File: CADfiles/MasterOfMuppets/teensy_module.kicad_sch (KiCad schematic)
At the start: 1 part, among them T1 Teensy4.1

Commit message: PCB Preps
Re-assigned footprints;
Placed all symbols in the middle;
Removed instruction to ignore the PCB in the README.manahmanah;
Added a generic placement recommendation file from Sir. Claude;
Ready to start the design;
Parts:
- T1: footprint teensy.pretty-master:Teensy41 -> Teensy:Teensy41
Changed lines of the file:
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@@
 			)
 		)
-		(property "Footprint" "teensy.pretty-master:Teensy41"
+		(property "Footprint" "Teensy:Teensy41"
 			(at 87.63 105.41 0)
 			(effects

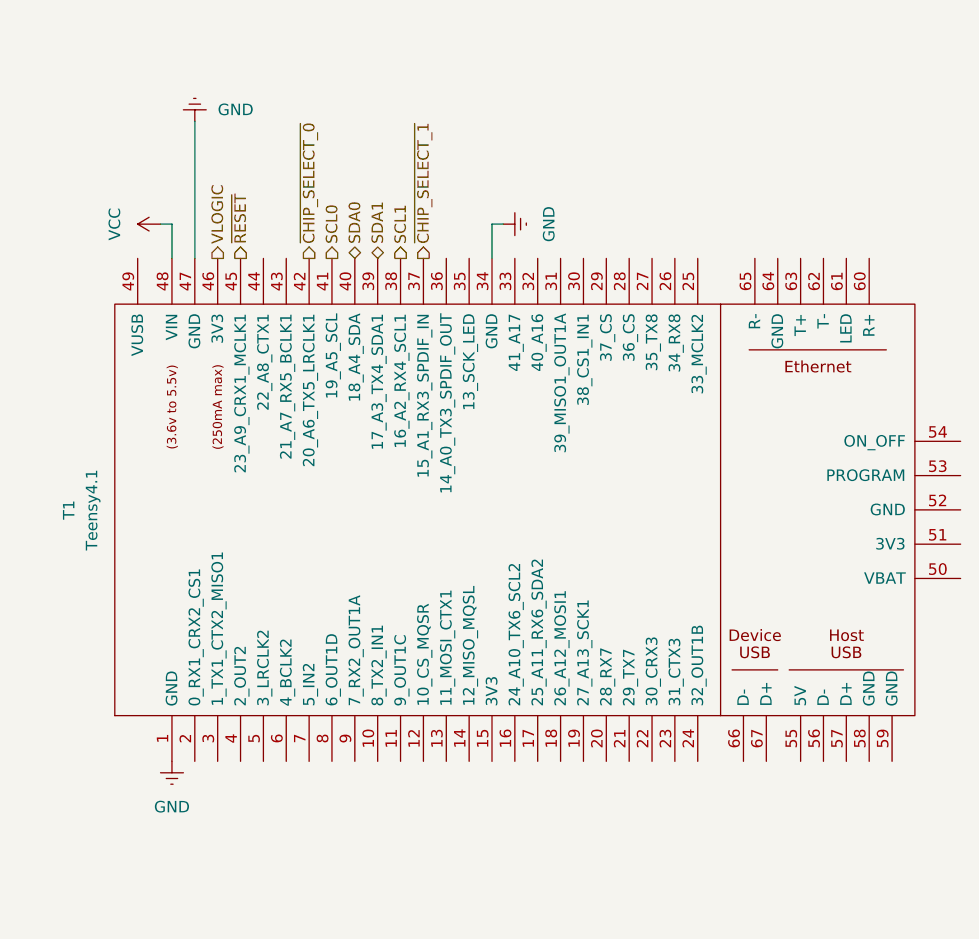
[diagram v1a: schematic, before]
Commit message: Pin configuration
The current prototype board has DAC0 mapped to Wire2 and DAC1 mapped to Wire1. The schematics were updated to reflect it.
Added chip select in the firmware for AD5593R using the address pin as a selector.
Next steps: update Claude's knowledge about it.
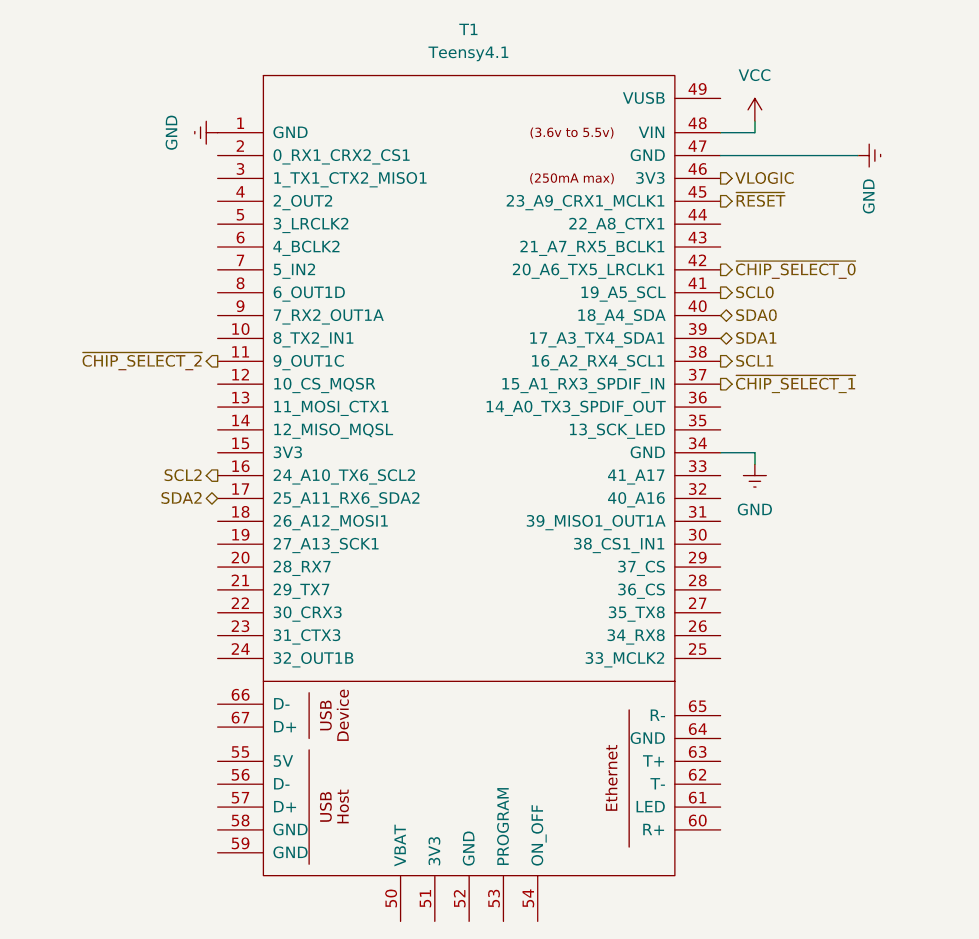
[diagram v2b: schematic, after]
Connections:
- net ~{CHIP_SELECT_2}: now reaches T1.11 (9_OUT1C)
- net SCL2: now reaches T1.16 (24_A10_TX6_SCL2)
- net SDA2: now reaches T1.17 (25_A11_RX6_SDA2)
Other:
- moved on the sheet: T1
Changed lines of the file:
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@@
 	(wire
 		(pts
-			(xy 43.18 63.5) (xy 43.18 67.31)
+			(xy 107.95 53.34) (xy 104.14 53.34)
 		)
 		(stroke
@@
 	(wire
 		(pts
-			(xy 45.72 52.07) (xy 45.72 67.31)
+			(xy 119.38 55.88) (xy 104.14 55.88)
 		)
 		(stroke
@@
 	(wire
 		(pts
-			(xy 78.74 63.5) (xy 80.01 63.5)
+			(xy 107.95 88.9) (xy 107.95 90.17)
 		)
 		(stroke
@@
 	(wire
 		(pts
-			(xy 78.74 67.31) (xy 78.74 63.5)
+			(xy 104.14 88.9) (xy 107.95 88.9)
 		)
 		(stroke
@@
 	(wire
 		(pts
-			(xy 41.91 63.5) (xy 43.18 63.5)
+			(xy 107.95 52.07) (xy 107.95 53.34)
 		)
 		(stroke
@@
 	(hierarchical_label "SDA0"
 		(shape bidirectional)
-		(at 63.5 67.31 90)
+		(at 104.14 73.66 0)
 		(effects
 			(font
@@
 	(hierarchical_label "~{RESET}"
 		(shape output)
-		(at 50.8 67.31 90)
+		(at 104.14 60.96 0)
 		(effects
 			(font
@@
 	(hierarchical_label "VLOGIC"
 		(shape output)
-		(at 48.26 67.31 90)
+		(at 104.14 58.42 0)
 		(effects
 			(font
@@
 	(hierarchical_label "SCL0"
 		(shape output)
-		(at 60.96 67.31 90)
+		(at 104.14 71.12 0)
 		(effects
 			(font
@@
 	(hierarchical_label "SDA1"
 		(shape bidirectional)
-		(at 66.04 67.31 90)
-		(effects
-			(font
-				(size 1.27 1.27)
-			)
-			(justify left)
+		(at 104.14 76.2 0)
+		(effects
+			(font
+				(size 1.27 1.27)
+			)
+			(justify left)
+		)
+	)
+	(hierarchical_label "SDA2"
+		(shape bidirectional)
+		(at 48.26 93.98 180)
+		(effects
+			(font
+				(size 1.27 1.27)
+			)
+			(justify right)
+		)
+	)
+	(hierarchical_label "SCL2"
+		(shape output)
+		(at 48.26 91.44 180)
+		(effects
+			(font
+				(size 1.27 1.27)
+			)
+			(justify right)
 		)
 	)
 	(hierarchical_label "~{CHIP_SELECT_1}"
 		(shape output)
-		(at 71.12 67.31 90)
+		(at 104.14 81.28 0)
 		(effects
 			(font
@@
 	(hierarchical_label "~{CHIP_SELECT_0}"
 		(shape output)
-		(at 58.42 67.31 90)
-		(effects
-			(font
-				(size 1.27 1.27)
-			)
-			(justify left)
+		(at 104.14 68.58 0)
+		(effects
+			(font
+				(size 1.27 1.27)
+			)
+			(justify left)
+		)
+	)
+	(hierarchical_label "~{CHIP_SELECT_2}"
+		(shape output)
+		(at 48.26 78.74 180)
+		(effects
+			(font
+				(size 1.27 1.27)
+			)
+			(justify right)
 		)
 	)
 	(hierarchical_label "SCL1"
 		(shape output)
-		(at 68.58 67.31 90)
+		(at 104.14 78.74 0)
 		(effects
 			(font
@@
 	(symbol
 		(lib_id "power:GNDREF")
-		(at 45.72 52.07 180)
+		(at 119.38 55.88 90)
 		(unit 1)
 		(exclude_from_sim no)
@@
 		(fields_autoplaced yes)
 		(property "Reference" "#PWR09"
-			(at 45.72 45.72 0)
+			(at 125.73 55.88 0)
 			(effects
 				(font
@@
 		)
 		(property "Value" "GND"
-			(at 48.26 50.7999 0)
+			(at 120.6501 58.42 0)
 			(effects
 				(font
@@
 		)
 		(property "Footprint" ""
-			(at 45.72 52.07 0)
+			(at 119.38 55.88 0)
 			(effects
 				(font
@@
 		)
 		(property "Datasheet" ""
-			(at 45.72 52.07 0)
+			(at 119.38 55.88 0)
 			(effects
 				(font
@@
 		)
 		(property "Description" "Power symbol creates a global label with name \"GNDREF\" , reference supply ground"
-			(at 45.72 52.07 0)
+			(at 119.38 55.88 0)
 			(effects
 				(font
@@
 	(symbol
 		(lib_id "teensy:Teensy4.1")
-		(at 97.79 95.25 90)
+		(at 76.2 107.95 0)
 		(unit 1)
 		(exclude_from_sim no)
@@
 		(fields_autoplaced yes)
 		(property "Reference" "T1"
-			(at 31.75 95.25 0)
+			(at 76.2 41.91 0)
 			(effects
 				(font
@@
 		)
 		(property "Value" "Teensy4.1"
-			(at 34.29 95.25 0)
+			(at 76.2 44.45 0)
 			(effects
 				(font
@@
 		)
 		(property "Footprint" "Teensy:Teensy41"
-			(at 87.63 105.41 0)
+			(at 66.04 97.79 0)
 			(effects
 				(font
@@
 		)
 		(property "Datasheet" ""
-			(at 87.63 105.41 0)
+			(at 66.04 97.79 0)
 			(effects
 				(font
@@
 		)
 		(property "Description" ""
-			(at 97.79 95.25 0)
+			(at 76.2 107.95 0)
 			(effects
 				(font
@@
 		)
 		(property "Manufacturer" ""
-			(at 97.79 95.25 0)
+			(at 76.2 107.95 0)
 			(effects
 				(font
@@
 		)
 		(property "Part Number" ""
-			(at 97.79 95.25 0)
+			(at 76.2 107.95 0)
 			(effects
 				(font
@@
 		)
 		(property "Specifications" ""
-			(at 97.79 95.25 0)
+			(at 76.2 107.95 0)
 			(effects
 				(font
@@
 	(symbol
 		(lib_id "power:GNDREF")
-		(at 80.01 63.5 90)
+		(at 107.95 90.17 0)
 		(unit 1)
 		(exclude_from_sim no)
@@
 		(fields_autoplaced yes)
 		(property "Reference" "#PWR010"
-			(at 86.36 63.5 0)
+			(at 107.95 96.52 0)
 			(effects
 				(font
@@
 		)
 		(property "Value" "GND"
-			(at 85.09 63.5 0)
+			(at 107.95 95.25 0)
 			(effects
 				(font
@@
 		)
 		(property "Footprint" ""
-			(at 80.01 63.5 0)
+			(at 107.95 90.17 0)
 			(effects
 				(font
@@
 		)
 		(property "Datasheet" ""
-			(at 80.01 63.5 0)
+			(at 107.95 90.17 0)
 			(effects
 				(font
@@
 		)
 		(property "Description" "Power symbol creates a global label with name \"GNDREF\" , reference supply ground"
-			(at 80.01 63.5 0)
+			(at 107.95 90.17 0)
 			(effects
 				(font
@@
 	(symbol
 		(lib_id "power:+5V")
-		(at 41.91 63.5 90)
+		(at 107.95 52.07 0)
 		(unit 1)
 		(exclude_from_sim no)
@@
 		(fields_autoplaced yes)
 		(property "Reference" "#PWR07"
-			(at 45.72 63.5 0)
+			(at 107.95 55.88 0)
 			(effects
 				(font
@@
 		)
 		(property "Value" "VCC"
-			(at 36.83 63.5 0)
+			(at 107.95 46.99 0)
 			(effects
 				(font
@@
 		)
 		(property "Footprint" ""
-			(at 41.91 63.5 0)
+			(at 107.95 52.07 0)
 			(effects
 				(font
@@
 		)
 		(property "Datasheet" ""
-			(at 41.91 63.5 0)
+			(at 107.95 52.07 0)
 			(effects
 				(font
@@
 		)
 		(property "Description" "Power symbol creates a global label with name \"+5V\""
-			(at 41.91 63.5 0)
+			(at 107.95 52.07 0)
 			(effects
 				(font
@@
 	(symbol
 		(lib_id "power:GNDREF")
-		(at 43.18 123.19 0)
+		(at 48.26 53.34 270)
 		(unit 1)
 		(exclude_from_sim no)
@@
 		(fields_autoplaced yes)
 		(property "Reference" "#PWR08"
-			(at 43.18 129.54 0)
+			(at 41.91 53.34 0)
 			(effects
 				(font
@@
 		)
 		(property "Value" "GND"
-			(at 43.18 128.27 0)
+			(at 43.18 53.34 0)
 			(effects
 				(font
@@
 		)
 		(property "Footprint" ""
-			(at 43.18 123.19 0)
+			(at 48.26 53.34 0)
 			(effects
 				(font
@@
 		)
 		(property "Datasheet" ""
-			(at 43.18 123.19 0)
+			(at 48.26 53.34 0)
 			(effects
 				(font
@@
 		)
 		(property "Description" "Power symbol creates a global label with name \"GNDREF\" , reference supply ground"
-			(at 43.18 123.19 0)
-			(effects
-				(font
+			(at 48.26 53.34 0)
+			(effects
+				(font
